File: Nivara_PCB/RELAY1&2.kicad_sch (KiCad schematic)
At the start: 0 parts

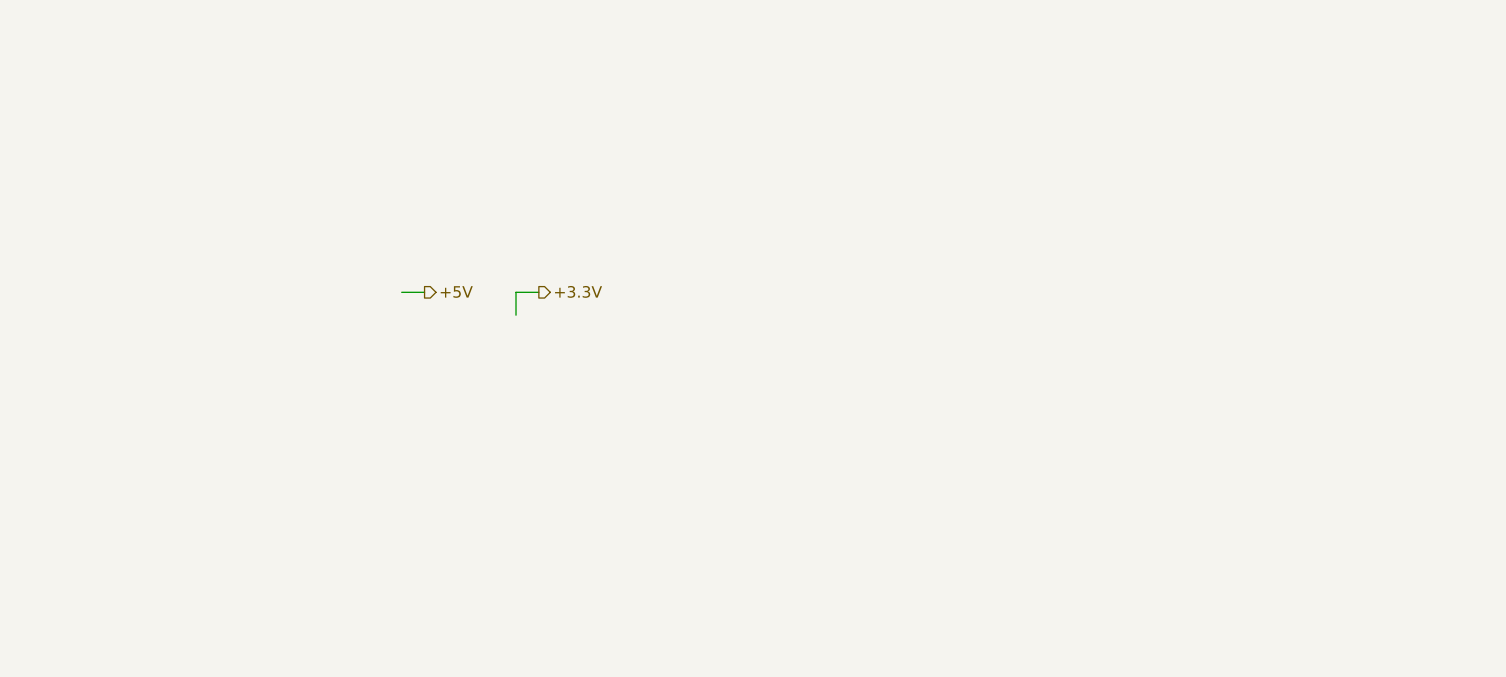
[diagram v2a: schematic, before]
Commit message: Cambios en el esquema de NPN y PNP
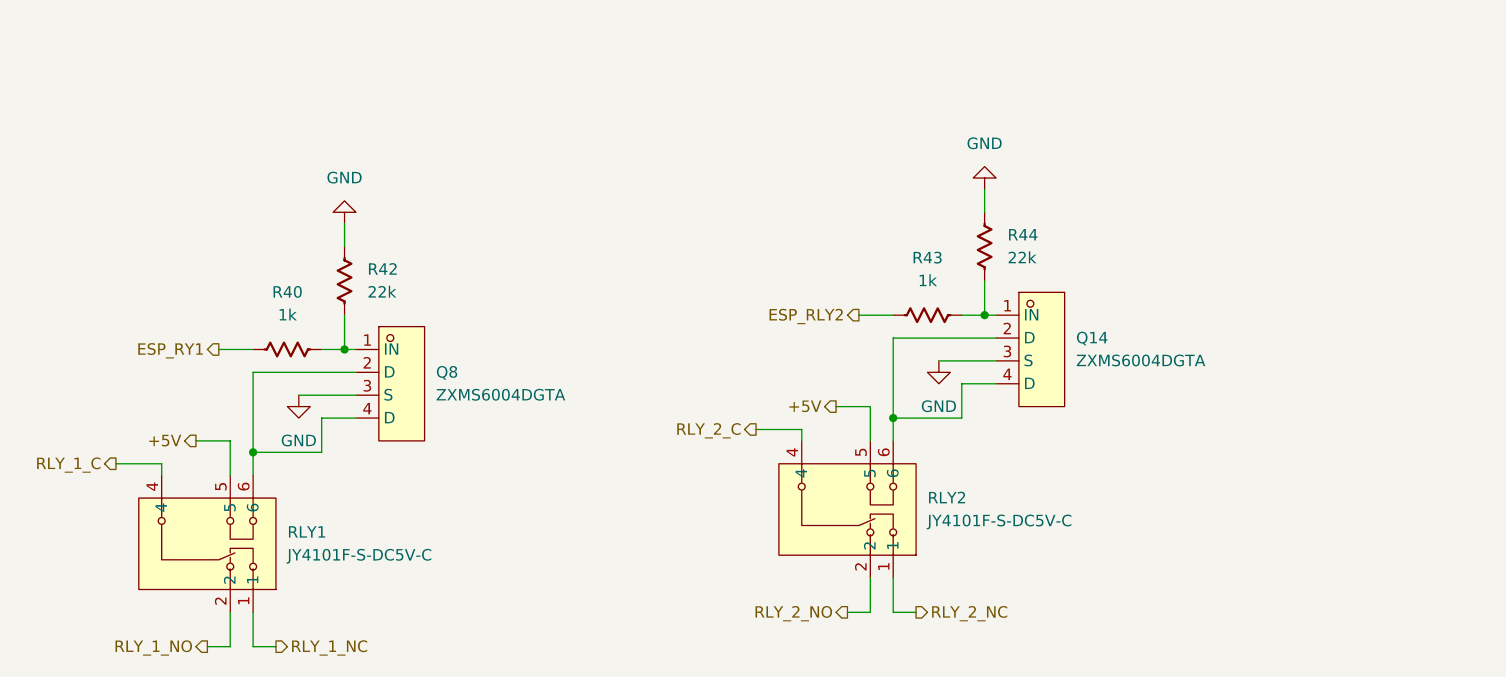
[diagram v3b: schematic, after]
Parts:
- added Q14, Q8: ZXMS6004DGTA, Fuse_Holder:SOT-223-3_L6.5-W3.4-P2.30-LS7.0-BR, symbol Fuse_Holder:ZXMS6004DGTA
- added R40, R43: 1k, PCM_Resistor_SMD_AKL:R_0603_1608Metric, symbol PCM_Resistor_US_AKL:R_0603
- added R42, R44: 22k, PCM_Resistor_SMD_AKL:R_0603_1608Metric, symbol PCM_Resistor_US_AKL:R_0603
- added RLY1, RLY2: JY4101F-S-DC5V-C, Fuse_Holder:RELAY-TH_HK4101F-XX-XX_XX, symbol Fuse_Holder:JY4101F-S-DC5V-C
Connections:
- net +5V: now also RLY1.5, RLY2.5
- new net: Q8.1 (IN), R40.2, R42.1
- new net: Q14.1 (IN), R43.2, R44.1
- new net: Q8.2 (D), Q8.4 (D), RLY1.6
- new net: Q14.2 (D), Q14.4 (D), RLY2.6
- new net ESP_RLY2: R43.1
- new net ESP_RY1: R40.1
- new net GND: Q14.3 (S), Q8.3 (S), R42.2, R44.2
- new net RLY_1_C: RLY1.4
- new net RLY_1_NC: RLY1.1
- new net RLY_1_NO: RLY1.2
- new net RLY_2_C: RLY2.4
- new net RLY_2_NC: RLY2.1
- new net RLY_2_NO: RLY2.2

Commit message: Cambio de IntelliFet, porque los que tenían no estaban disponibles.
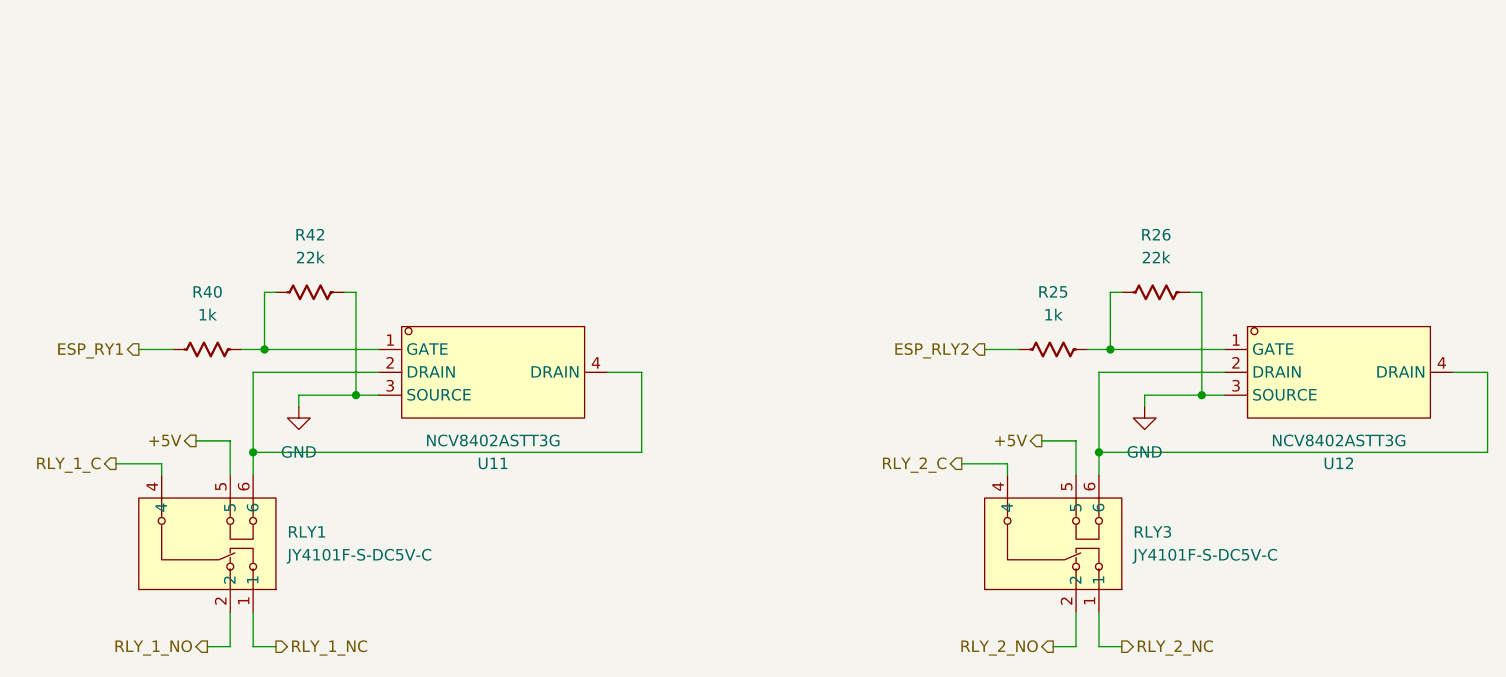
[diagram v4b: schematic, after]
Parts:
- removed Q14, Q8: ZXMS6004DGTA, Fuse_Holder:SOT-223-3_L6.5-W3.4-P2.30-LS7.0-BR, symbol Fuse_Holder:ZXMS6004DGTA
- removed R43: 1k, PCM_Resistor_SMD_AKL:R_0603_1608Metric, symbol PCM_Resistor_US_AKL:R_0603
- removed R44: 22k, PCM_Resistor_SMD_AKL:R_0603_1608Metric, symbol PCM_Resistor_US_AKL:R_0603
- removed RLY2: JY4101F-S-DC5V-C, Fuse_Holder:RELAY-TH_HK4101F-XX-XX_XX, symbol Fuse_Holder:JY4101F-S-DC5V-C
- added R25: 1k, PCM_Resistor_SMD_AKL:R_0603_1608Metric, symbol PCM_Resistor_US_AKL:R_0603
- added R26: 22k, PCM_Resistor_SMD_AKL:R_0603_1608Metric, symbol PCM_Resistor_US_AKL:R_0603
- added RLY3: JY4101F-S-DC5V-C, Fuse_Holder:RELAY-TH_HK4101F-XX-XX_XX, symbol Fuse_Holder:JY4101F-S-DC5V-C
- added U11, U12: NCV8402ASTT3G, Fuse_Holder:SOT-223_L6.5-W3.5-P2.30-LS7.0-BR, symbol Fuse_Holder:NCV8402ASTT3G
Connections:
- net +5V: now also RLY3.5
- net ESP_RLY2: now also R25.1
- net GND: now also R42.1, R26.1, U11.3 (SOURCE), U12.3 (SOURCE); no longer R42.2
- net RLY_2_C: now also RLY3.4
- net RLY_2_NC: now also RLY3.1
- net RLY_2_NO: now also RLY3.2
- net at R40.2: now also R42.2, U11.1 (GATE); no longer R42.1
- net at RLY1.6: now also U11.2 (DRAIN), U11.4 (DRAIN)
- new net: R25.2, R26.2, U12.1 (GATE)
- new net: RLY3.6, U12.2 (DRAIN), U12.4 (DRAIN)
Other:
- moved on the sheet: R40, R42

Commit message: Cambios en las salidas analogicas, ya que el ESP32 S3 no tiene DAC
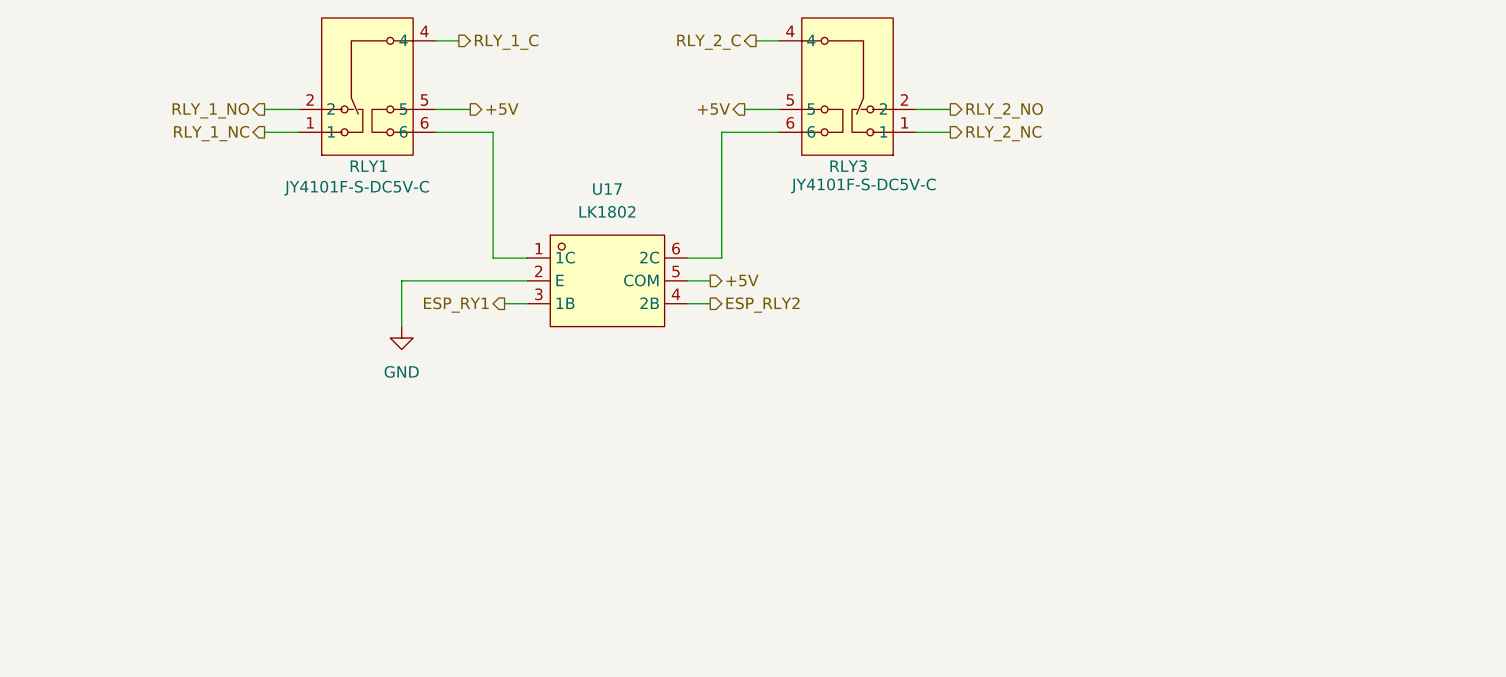
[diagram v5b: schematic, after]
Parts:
- removed R25, R40: 1k, PCM_Resistor_SMD_AKL:R_0603_1608Metric, symbol PCM_Resistor_US_AKL:R_0603
- removed R26, R42: 22k, PCM_Resistor_SMD_AKL:R_0603_1608Metric, symbol PCM_Resistor_US_AKL:R_0603
- removed U11, U12: NCV8402ASTT3G, Fuse_Holder:SOT-223_L6.5-W3.5-P2.30-LS7.0-BR, symbol Fuse_Holder:NCV8402ASTT3G
- added U17: LK1802, EasyEDA:SOT-23-6_L2.9-W1.6-P0.95-LS2.8-BR, symbol EasyEDA:LK1802
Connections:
- net +5V: now also U17.5 (COM)
- net ESP_RLY2: now also U17.4 (2B)
- net ESP_RY1: now also U17.3 (1B)
- net GND: now also U17.2 (E)
- net at RLY3.6: now also U17.6 (2C)
- net at RLY1.6: now also U17.1 (1C)
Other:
- moved on the sheet: RLY1, RLY3
